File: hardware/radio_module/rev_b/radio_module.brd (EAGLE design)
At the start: 68.1 x 66 mm, 130 parts, among them J1 MODULE_GENERIC, J2 TC2030-JLINK-NL, J4 NANO_SIM, J5 TC2030-JLINK-L, P1 MOLEX_73251-135X, P2 MOLEX_73251-135X, Q1 MOSFET-NCHANNELSMD, Q2 MOSFET-NCHANNELSMD, Q3 MOSFET-NCHANNELSMD, Q5 SI223DDS, Q6 SI223DDS, Q7 SI223DDS, Q8 MOSFET-NCHANNELSMD, U1 NUCLEUM, U11 SAM4LC8BA, U12 UBLOX_SARA_G350, U2 TLV62130, U3 TXB0104RUT, U4 LTC2941, U5 LTC2941, U6 IM880_MODULE, U7 PCA9544AQFN-N20, U8 TLV62130, U9 LTC2941, X2 16 MHz

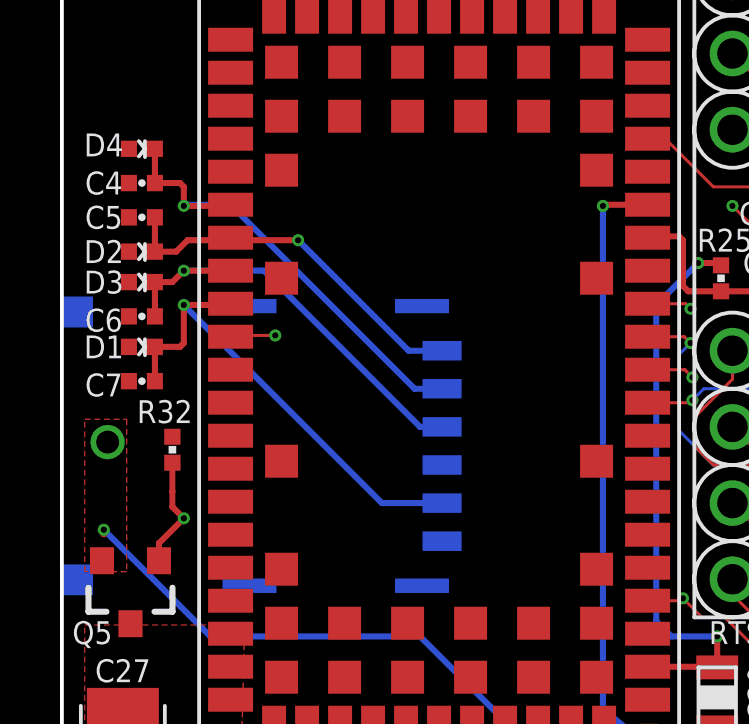
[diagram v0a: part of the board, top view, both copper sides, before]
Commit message: fixed the SIM card part (it was backwards)
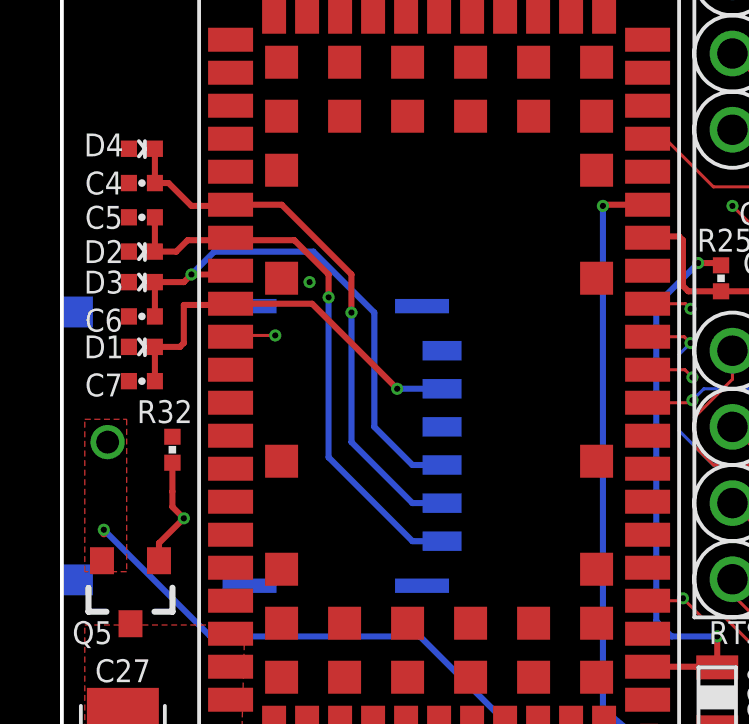
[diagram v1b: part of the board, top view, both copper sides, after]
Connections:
- removed net ADVREFP: U11.24
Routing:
- net N$3: track 12.5 -> 18.7 mm
- net N$2: track 14.6 -> 18.3 mm
- net N$1: track 16.4 -> 13.2 mm
- net N$4: track 15.5 -> 18.4 mm
- net GND: vias 122 -> 123
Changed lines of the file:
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@@
 <setting verticaltext="up"/>
 </settings>
-<grid distance="0.0025" unitdist="inch" unit="inch" style="lines" multiple="1" display="yes" altdistance="0.01" altunitdist="inch" altunit="inch"/>
+<grid distance="0.01" unitdist="inch" unit="inch" style="lines" multiple="1" display="yes" altdistance="0.01" altunitdist="inch" altunit="inch"/>
 <layers>
 <layer number="1" name="Top" color="4" fill="1" visible="yes" active="yes"/>
@@
 <layer number="57" name="tCAD" color="7" fill="1" visible="no" active="no"/>
 <layer number="59" name="Invisible" color="7" fill="1" visible="no" active="no"/>
+<layer number="60" name="bCarbon" color="7" fill="1" visible="no" active="no"/>
 <layer number="61" name="stand" color="7" fill="1" visible="no" active="no"/>
+<layer number="90" name="Modules" color="5" fill="1" visible="no" active="no"/>
 <layer number="91" name="Nets" color="2" fill="1" visible="no" active="no"/>
 <layer number="92" name="Busses" color="1" fill="1" visible="no" active="no"/>
@@
 <layer number="113" name="IDFDebug" color="7" fill="1" visible="no" active="yes"/>
 <layer number="116" name="Patch_BOT" color="9" fill="4" visible="no" active="yes"/>
+<layer number="118" name="Rect_Pads" color="7" fill="1" visible="yes" active="yes"/>
 <layer number="121" name="_tsilk" color="7" fill="1" visible="no" active="yes"/>
 <layer number="122" name="_bsilk" color="7" fill="1" visible="no" active="yes"/>
@@
 <layer number="127" name="_tValues" color="7" fill="1" visible="no" active="yes"/>
 <layer number="128" name="_bValues" color="7" fill="1" visible="no" active="yes"/>
+<layer number="129" name="Mask" color="7" fill="1" visible="yes" active="yes"/>
 <layer number="130" name="bLogo" color="7" fill="1" visible="yes" active="yes"/>
 <layer number="131" name="tAdjust" color="7" fill="1" visible="yes" active="yes"/>
@@
 <layer number="223" name="223bmp" color="24" fill="1" visible="no" active="no"/>
 <layer number="224" name="224bmp" color="25" fill="1" visible="no" active="no"/>
+<layer number="225" name="225bmp" color="7" fill="1" visible="yes" active="yes"/>
+<layer number="226" name="226bmp" color="7" fill="1" visible="yes" active="yes"/>
+<layer number="227" name="227bmp" color="7" fill="1" visible="yes" active="yes"/>
+<layer number="228" name="228bmp" color="7" fill="1" visible="yes" active="yes"/>
+<layer number="229" name="229bmp" color="7" fill="1" visible="yes" active="yes"/>
+<layer number="230" name="230bmp" color="7" fill="1" visible="yes" active="yes"/>
 <layer number="231" name="Eagle3D_PG1" color="14" fill="1" visible="yes" active="yes"/>
 <layer number="232" name="Eagle3D_PG2" color="14" fill="2" visible="yes" active="yes"/>
@@
 <layer number="251" name="SMDround" color="12" fill="11" visible="no" active="no"/>
 <layer number="254" name="cooling" color="7" fill="1" visible="no" active="yes"/>
+<layer number="255" name="routoute" color="7" fill="1" visible="yes" active="yes"/>
 </layers>
 <board>
@@
 <attribute name="NAME" x="41.529" y="44.624" size="0.762" layer="25" font="vector" align="bottom-center"/>
 <attribute name="VALUE" x="36.449" y="45.497" size="0.8128" layer="27" font="vector" ratio="12" rot="R180" align="bottom-center"/>
-<attribute name="DIGIKEY" value="ATSAM4LC8BA-MURDKR-ND" x="36.449" y="39.497" size="1.778" layer="27" rot="R180" display="off"/>
+<attribute name="DIGIKEY" value="ATSAM4LC8BA-MURCT-ND" x="36.449" y="39.497" size="1.778" layer="27" rot="R180" display="off"/>
 </element>
 <element name="U5" library="signpost" package="DFN-6-2MMX3MM" value="LTC2941" x="49.657" y="51.816" smashed="yes" rot="R270">
@@
 <contactref element="D1" pad="CATHODE"/>
 <contactref element="C7" pad="1"/>
-<via x="6.858" y="39.116" extent="1-16" drill="0.2032"/>
 <wire x1="6.858" y1="39.116" x2="8.376" y2="39.116" width="0.2032" layer="1"/>
 <wire x1="8.376" y1="39.116" x2="8.417" y2="39.157" width="0.2032" layer="1"/>
@@
 <wire x1="6.858" y1="37.846" x2="6.731" y2="37.719" width="0.2032" layer="1"/>
 <wire x1="6.731" y1="37.719" x2="5.89406875" y2="37.719" width="0.2032" layer="1"/>
-<wire x1="15.468" y1="32.512" x2="13.462" y2="32.512" width="0.2032" layer="16"/>
-<wire x1="13.462" y1="32.512" x2="6.858" y2="39.116" width="0.2032" layer="16"/>
+<wire x1="8.417" y1="39.157" x2="11.135" y2="39.157" width="0.2032" layer="1"/>
+<wire x1="11.135" y1="39.157" x2="13.97" y2="36.322" width="0.2032" layer="1"/>
+<via x="13.97" y="36.322" extent="1-16" drill="0.2032"/>
+<wire x1="13.97" y1="36.322" x2="15.468" y2="36.322" width="0.2032" layer="16"/>
 </signal>
 <signal name="N$2">
@@
 <contactref element="C6" pad="1"/>
 <wire x1="5.89406875" y1="38.735" x2="5.89406875" y2="39.878" width="0.2032" layer="1"/>
-<via x="6.858" y="40.259" extent="1-16" drill="0.2032"/>
-<wire x1="6.858" y1="40.259" x2="8.415" y2="40.259" width="0.2032" layer="1"/>
-<wire x1="8.415" y1="40.259" x2="8.417" y2="40.257" width="0.2032" layer="1"/>
-<wire x1="6.858" y1="40.259" x2="6.477" y2="39.878" width="0.2032" layer="1"/>
-<wire x1="6.477" y1="39.878" x2="5.89406875" y2="39.878" width="0.2032" layer="1"/>
-<wire x1="6.858" y1="40.259" x2="9.525" y2="40.259" width="0.2032" layer="16"/>
-<wire x1="9.525" y1="40.259" x2="14.732" y2="35.052" width="0.2032" layer="16"/>
-<wire x1="14.732" y1="35.052" x2="15.468" y2="35.052" width="0.2032" layer="16"/>
+<wire x1="5.89406875" y1="39.878" x2="6.858" y2="39.878" width="0.2032" layer="1"/>
+<wire x1="6.858" y1="39.878" x2="7.112" y2="40.132" width="0.2032" layer="1"/>
+<wire x1="7.874" y1="40.132" x2="8.292" y2="40.132" width="0.2032" layer="1"/>
+<wire x1="8.292" y1="40.132" x2="8.417" y2="40.257" width="0.2032" layer="1"/>
+<wire x1="8.417" y1="40.257" x2="7.999" y2="40.257" width="0.2032" layer="1"/>
+<wire x1="7.999" y1="40.257" x2="7.874" y2="40.132" width="0.2032" layer="1"/>
+<wire x1="7.874" y1="40.132" x2="7.112" y2="40.132" width="0.2032" layer="1"/>
+<via x="7.112" y="40.132" extent="1-16" drill="0.2032"/>
+<wire x1="7.112" y1="40.132" x2="7.874" y2="40.894" width="0.2032" layer="16"/>
+<wire x1="7.874" y1="40.894" x2="11.176" y2="40.894" width="0.2032" layer="16"/>
+<wire x1="11.176" y1="40.894" x2="13.208" y2="38.862" width="0.2032" layer="16"/>
+<wire x1="13.208" y1="38.862" x2="13.208" y2="35.052" width="0.2032" layer="16"/>
+<wire x1="13.208" y1="35.052" x2="14.478" y2="33.782" width="0.2032" layer="16"/>
+<wire x1="14.478" y1="33.782" x2="15.468" y2="33.782" width="0.2032" layer="16"/>
 </signal>
 <signal name="N$3">
@@
 <contactref element="C5" pad="1"/>
 <wire x1="5.89406875" y1="40.894" x2="5.89406875" y2="42.037" width="0.2032" layer="1"/>
-<via x="10.668" y="41.275" extent="1-16" drill="0.2032"/>
-<wire x1="10.668" y1="41.275" x2="8.335" y2="41.275" width="0.2032" layer="1"/>
 <wire x1="8.335" y1="41.275" x2="8.417" y2="41.357" width="0.2032" layer="1"/>
 <wire x1="5.89406875" y1="40.894" x2="6.604" y2="40.894" width="0.2032" layer="1"/>
 <wire x1="6.604" y1="40.894" x2="6.985" y2="41.275" width="0.2032" layer="1"/>
 <wire x1="6.985" y1="41.275" x2="8.335" y2="41.275" width="0.2032" layer="1"/>
-<wire x1="15.468" y1="37.592" x2="14.351" y2="37.592" width="0.2032" layer="16"/>
-<wire x1="14.351" y1="37.592" x2="10.668" y2="41.275" width="0.2032" layer="16"/>
+<wire x1="8.335" y1="41.275" x2="10.541" y2="41.275" width="0.2032" layer="1"/>
+<wire x1="10.541" y1="41.275" x2="11.684" y2="40.132" width="0.2032" layer="1"/>
+<wire x1="11.684" y1="40.132" x2="11.684" y2="39.37" width="0.2032" layer="1"/>
+<via x="11.684" y="39.37" extent="1-16" drill="0.2032"/>
+<wire x1="11.684" y1="39.37" x2="11.684" y2="34.036" width="0.2032" layer="16"/>
+<wire x1="11.684" y1="34.036" x2="14.478" y2="31.242" width="0.2032" layer="16"/>
+<wire x1="14.478" y1="31.242" x2="15.468" y2="31.242" width="0.2032" layer="16"/>
 </signal>
 <signal name="GND">
@@
 <wire x1="21.66493125" y1="21.32893125" x2="21.656" y2="21.32" width="0.1016" layer="1"/>
 <via x="28.194" y="30.099" extent="1-16" drill="0.2032"/>
+<via x="11.049" y="39.878" extent="1-16" drill="0.2032"/>
 </signal>
 <signal name="N$4">
@@
 <contactref element="C4" pad="1"/>
 <wire x1="5.89406875" y1="44.323" x2="5.89406875" y2="43.18" width="0.2032" layer="1"/>
-<via x="6.858" y="42.418" extent="1-16" drill="0.2032"/>
-<wire x1="6.858" y1="42.418" x2="8.378" y2="42.418" width="0.2032" layer="1"/>
+<wire x1="5.89406875" y1="43.18" x2="6.35" y2="43.18" width="0.2032" layer="1"/>
+<wire x1="6.35" y1="43.18" x2="7.112" y2="42.418" width="0.2032" layer="1"/>
+<wire x1="7.112" y1="42.418" x2="8.378" y2="42.418" width="0.2032" layer="1"/>
 <wire x1="8.378" y1="42.418" x2="8.417" y2="42.457" width="0.2032" layer="1"/>
-<wire x1="5.89406875" y1="43.18" x2="6.731" y2="43.18" width="0.2032" layer="1"/>
-<wire x1="6.731" y1="43.18" x2="6.858" y2="43.053" width="0.2032" layer="1"/>
-<wire x1="6.858" y1="43.053" x2="6.858" y2="42.418" width="0.2032" layer="1"/>
-<wire x1="15.468" y1="36.322" x2="14.552" y2="36.322" width="0.2032" layer="16"/>
-<wire x1="14.552" y1="36.322" x2="8.417" y2="42.457" width="0.2032" layer="16"/>
-<wire x1="8.417" y1="42.457" x2="6.897" y2="42.457" width="0.2032" layer="16"/>
-<wire x1="6.897" y1="42.457" x2="6.858" y2="42.418" width="0.2032" layer="16"/>
+<wire x1="8.417" y1="42.457" x2="10.121" y2="42.457" width="0.2032" layer="1"/>
+<wire x1="10.121" y1="42.457" x2="12.446" y2="40.132" width="0.2032" layer="1"/>
+<wire x1="12.446" y1="40.132" x2="12.446" y2="38.862" width="0.2032" layer="1"/>
+<via x="12.446" y="38.862" extent="1-16" drill="0.2032"/>
+<wire x1="12.446" y1="38.862" x2="12.446" y2="34.544" width="0.2032" layer="16"/>
+<wire x1="12.446" y1="34.544" x2="14.478" y2="32.512" width="0.2032" layer="16"/>
+<wire x1="14.478" y1="32.512" x2="15.468" y2="32.512" width="0.2032" layer="16"/>
 </signal>
 <signal name="N$6">
@@
 </signal>
 <signal name="ADVREFP">
-<contactref element="U11" pad="24"/>
 </signal>
 <signal name="USB_D-">

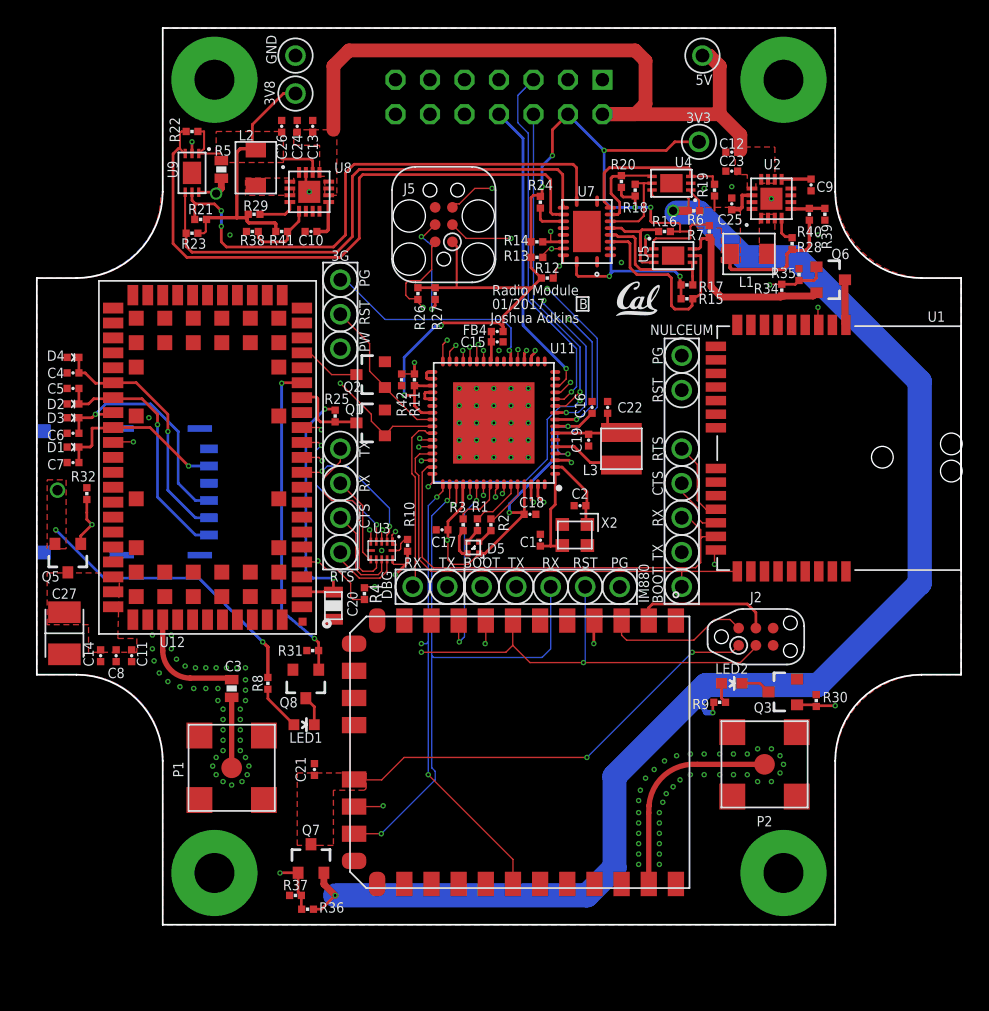
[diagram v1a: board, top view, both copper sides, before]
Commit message: added debug, positioning and routing
Still need to add programming signals to the debug header
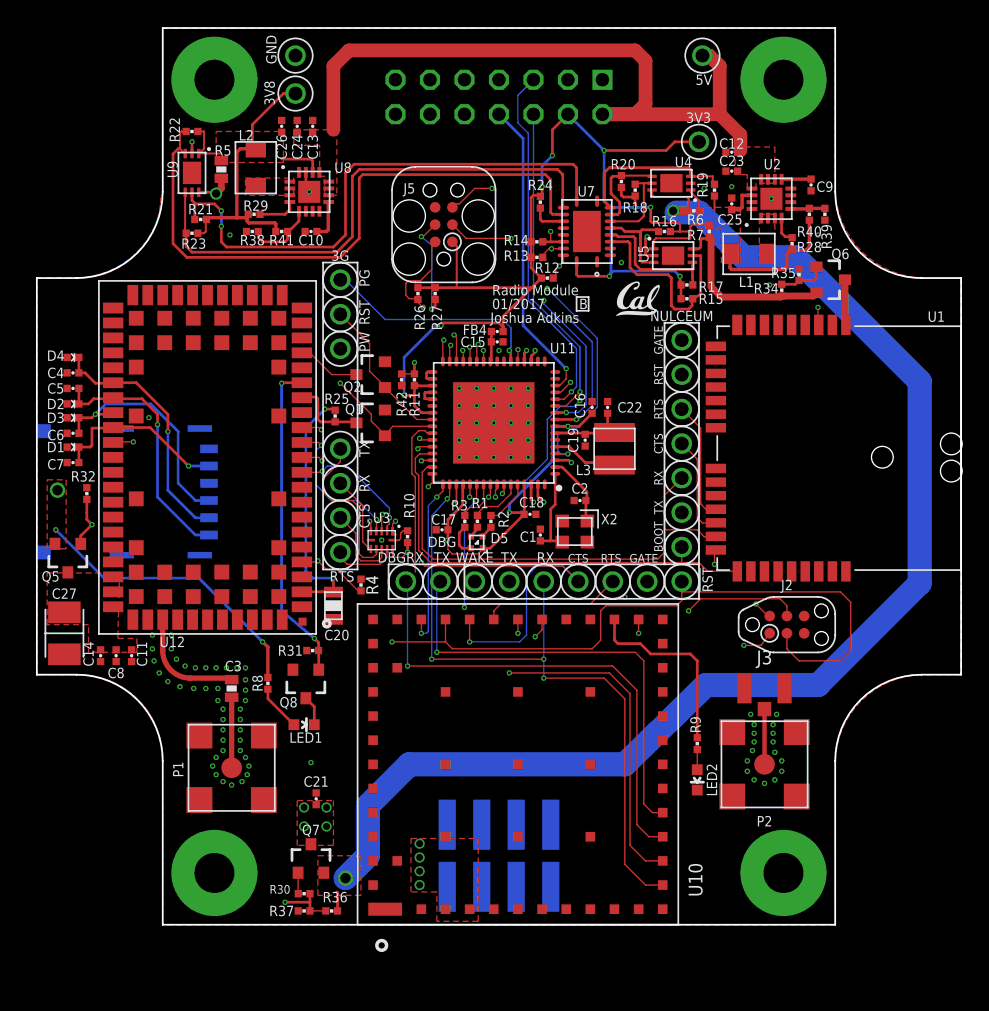
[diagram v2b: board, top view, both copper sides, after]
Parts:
- removed Q3: MOSFET-NCHANNELSMD, fets:SOT23-3
- removed TP20, TP8: TEST_POINT_0.040IN, headers:TESTPOINT_0.040IN
- removed U6: IM880_MODULE, chips:IM880_MODULE
- added J3: U.FL-R-SMT, connector:U.FL_SMT
- added TP26, TP27, TP28, TP29: TEST_POINT_0.040IN, headers:TESTPOINT_0.040IN
- added U10: XDOT_MODULE, signpost:XDOT_MODULE
- C21: value 1uF -> 10uF
- J1: value MODULE_GENERIC -> MODULE_GENERIC_DEBUGSMT; device signpost:MODULE_GENERIC -> signpost:MODULE_GENERIC_DEBUG_SMT
- R30: value 100k -> 100
- moved R30 40.3 mm to (22.5, 4.83), turned to 0 degrees
- moved LED2 7.55 mm to (51.4, 13.2), turned to 180 degrees
- moved TP7 7.12 mm to (50.3, 27.8)
- moved R9 3.47 mm to (51.4, 15.9), turned to 90 degrees
- moved TP11 2.92 mm to (50.3, 30.4)
- moved TP10 2.92 mm to (50.3, 38.0)
- moved TP12 2.92 mm to (50.3, 32.9)
- moved TP18 2.92 mm to (50.3, 35.4)
- moved TP9 2.92 mm to (50.3, 40.5)
- moved J2 2.45 mm to (58.0, 24.6)
- moved C21 2.16 mm to (23.4, 11.8)
- moved TP4 2.07 mm to (47.8, 27.8)
- moved R36 1.78 mm to (24.5, 3.56)
- moved R37 1.31 mm to (22.5, 3.56)
- moved TP19 1.14 mm to (50.3, 45.6)
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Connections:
- removed net !IM880_RESET: J2.3, TP7.TESTPOINT, U11.44, U6.7
- removed net IM880_3V3: Q7.2, R36.2, R6.1, R9.2, U4.6
- removed net IM880_BOOT: TP6.TESTPOINT, U11.49, U6.26
- removed net IM880_GATED: C21.1, J2.1, Q7.3, U6.17
- removed net IM880_INT1: U11.55, U6.8
- removed net IM880_INT2: U11.54, U6.9
- removed net IM880_NETWORK: Q3.1, R30.2, U6.4
- removed net IM880_POWER_GATE: Q7.1, R36.1, R37.2, TP4.TESTPOINT, U11.21
- removed net IM880_RX: TP1.TESTPOINT, U11.51, U6.18
- removed net IM880_SWCLK: J2.4, U6.2
- removed net IM880_SWDIO: J2.2, U6.3
- removed net IM880_TX: TP2.TESTPOINT, U11.50, U6.19
- new net !XDOT_RESET: J2.3, TP7.TESTPOINT, U10.P$33, U11.30
- new net XDOT_3V3: Q7.2, R36.2, R6.1, U4.6
- new net XDOT_DBG_UART_RX: TP29.TESTPOINT, U10.P$16
- new net XDOT_DBG_UART_TX: TP28.TESTPOINT, U10.P$15
- new net XDOT_GATED: C21.1, J2.1, Q7.3, U10.P$3, U10.P$4
- new net XDOT_GPIO0: R9.2, U10.P$26
- new net XDOT_HOST_UART_CTS: TP27.TESTPOINT, U10.P$32, U11.44
- new net XDOT_HOST_UART_RTS: TP26.TESTPOINT, U10.P$31, U11.56
- new net XDOT_HOST_UART_RX: TP1.TESTPOINT, U10.P$14, U11.51
- new net XDOT_HOST_UART_TX: TP2.TESTPOINT, U10.P$13, U11.50
- new net XDOT_INT1: U10.P$25, U11.54
- new net XDOT_POWER_GATE: R30.2, R36.1, R37.2, TP4.TESTPOINT, U11.21
- new net XDOT_SWCLK: J2.4, U10.P$29
- new net XDOT_SWDIO: J2.2, U10.P$30
- new net XDOT_WAKE: TP6.TESTPOINT, U10.P$34, U11.49
- net DEBUG_RX: now also J1.18; no longer TP20.TESTPOINT
- net DEBUG_TX: now also J1.17; no longer TP8.TESTPOINT
- net GND: now also J1.15, J3.GND1, J3.GND2, LED2.C, U10.P$1, U10.P$17, U10.P$20, U10.P$35, U10.P$36, U10.P$38, U10.P$39, U10.P$40, U10.P$41, U10.P$42, U10.P$43, U10.P$44, U10.P$45, U10.P$46, U10.P$48, U10.P$49, U10.P$5, U10.P$50, U10.P$51, U10.P$52, U10.P$53, U10.P$54, U10.P$55, U10.P$56, U10.P$57, U10.P$58; no longer Q3.2, R30.1, U6.1, U6.11, U6.16, U6.22, U6.27, U6.30, U6.32, U6.6
- net N$24: now also J3.SIG; no longer U6.31
- net N$26: now also U11.55; no longer U11.56
- net N$28: now also Q7.1, R30.1; no longer LED2.C, Q3.3
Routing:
- net IM880_3V3: track 106.9 -> 0.00 mm, vias 3 -> 0
- net XDOT_3V3: track 0.00 -> 98.3 mm, vias 0 -> 2
- net !XDOT_RESET: track 0.00 -> 84.3 mm, vias 0 -> 2
- net XDOT_POWER_GATE: track 0.00 -> 77.1 mm, vias 0 -> 3
- net IM880_POWER_GATE: track 67.3 -> 0.00 mm, vias 2 -> 0
- net XDOT_HOST_UART_TX: track 0.00 -> 51.0 mm, vias 0 -> 4
- net !IM880_RESET: track 50.3 -> 0.00 mm, vias 3 -> 0
- net XDOT_HOST_UART_RX: track 0.00 -> 48.6 mm, vias 0 -> 2
- net IM880_TX: track 43.7 -> 0.00 mm, vias 2 -> 0
- net IM880_BOOT: track 41.6 -> 0.00 mm, vias 3 -> 0
- net IM880_RX: track 39.5 -> 0.00 mm, vias 2 -> 0
- net XDOT_HOST_UART_CTS: track 0.00 -> 38.2 mm, vias 0 -> 3
- net XDOT_GATED: track 0.00 -> 38.0 mm, vias 0 -> 9
- net XDOT_DBG_UART_TX: track 0.00 -> 36.1 mm, vias 0 -> 1
- net XDOT_DBG_UART_RX: track 0.00 -> 33.0 mm, vias 0 -> 1
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- added copper zone on layer 1, net XDOT_3V3
- added copper zone on layer 1, net XDOT_GATED
- added copper zone on layer 2, net XDOT_GATED
- removed copper zone on layer 1, net IM880_GATED
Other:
- board text added: "!RST"
- board text added: "DBG TX"
- board text added: "DBGRX"
- board text added: "GATE"
- board text added: "WAKE"
- board text removed: "DBG"
- board text removed: "IM880"
